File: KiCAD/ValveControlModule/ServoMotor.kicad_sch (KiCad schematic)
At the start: 5 parts, among them J1 DF51A-4P-2DS, U2 LT1785xS8

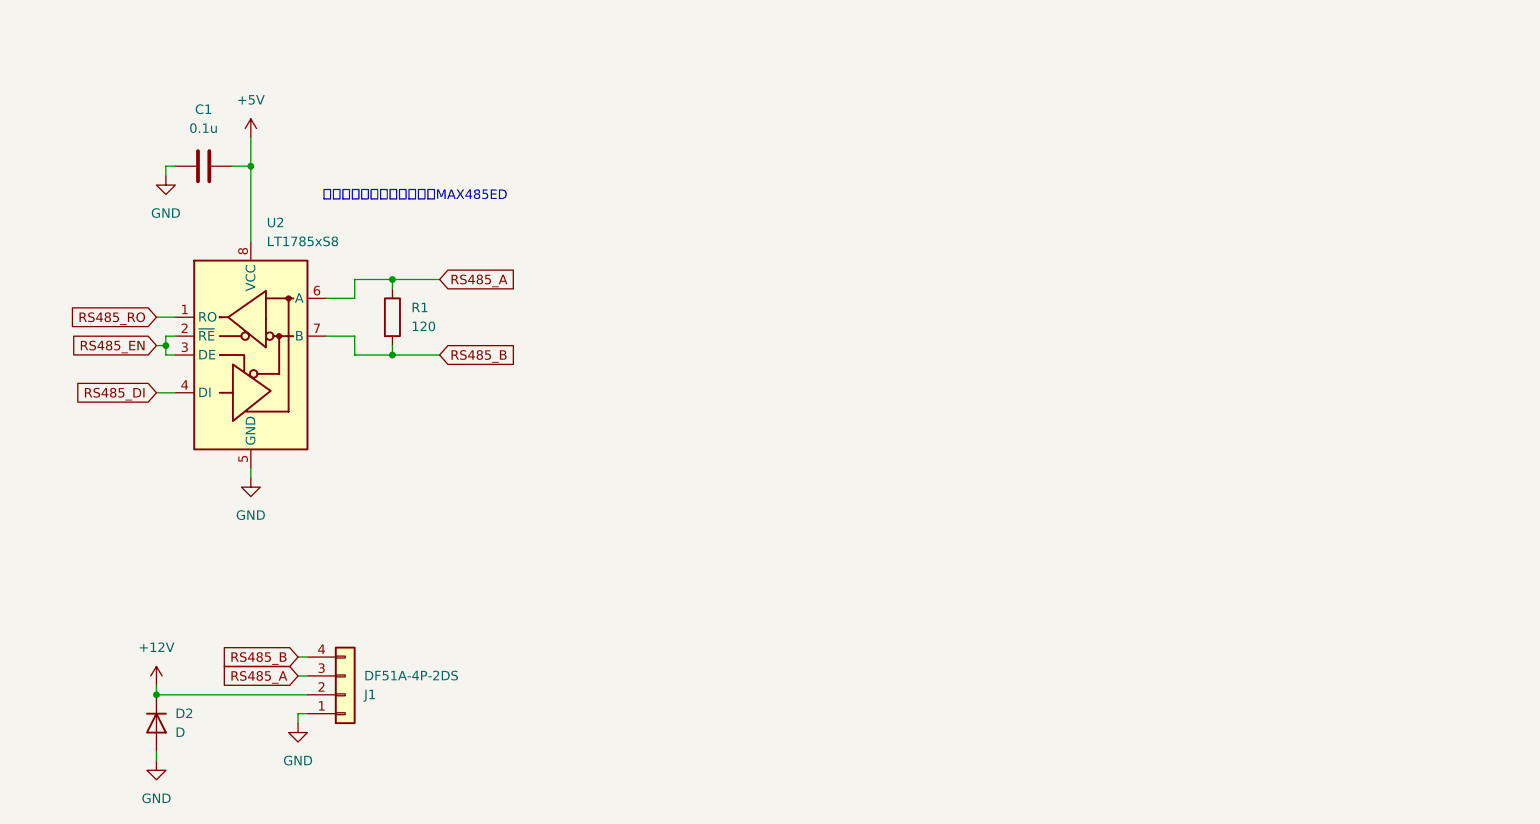
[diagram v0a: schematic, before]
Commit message: 電源，RS485の仕様を確定
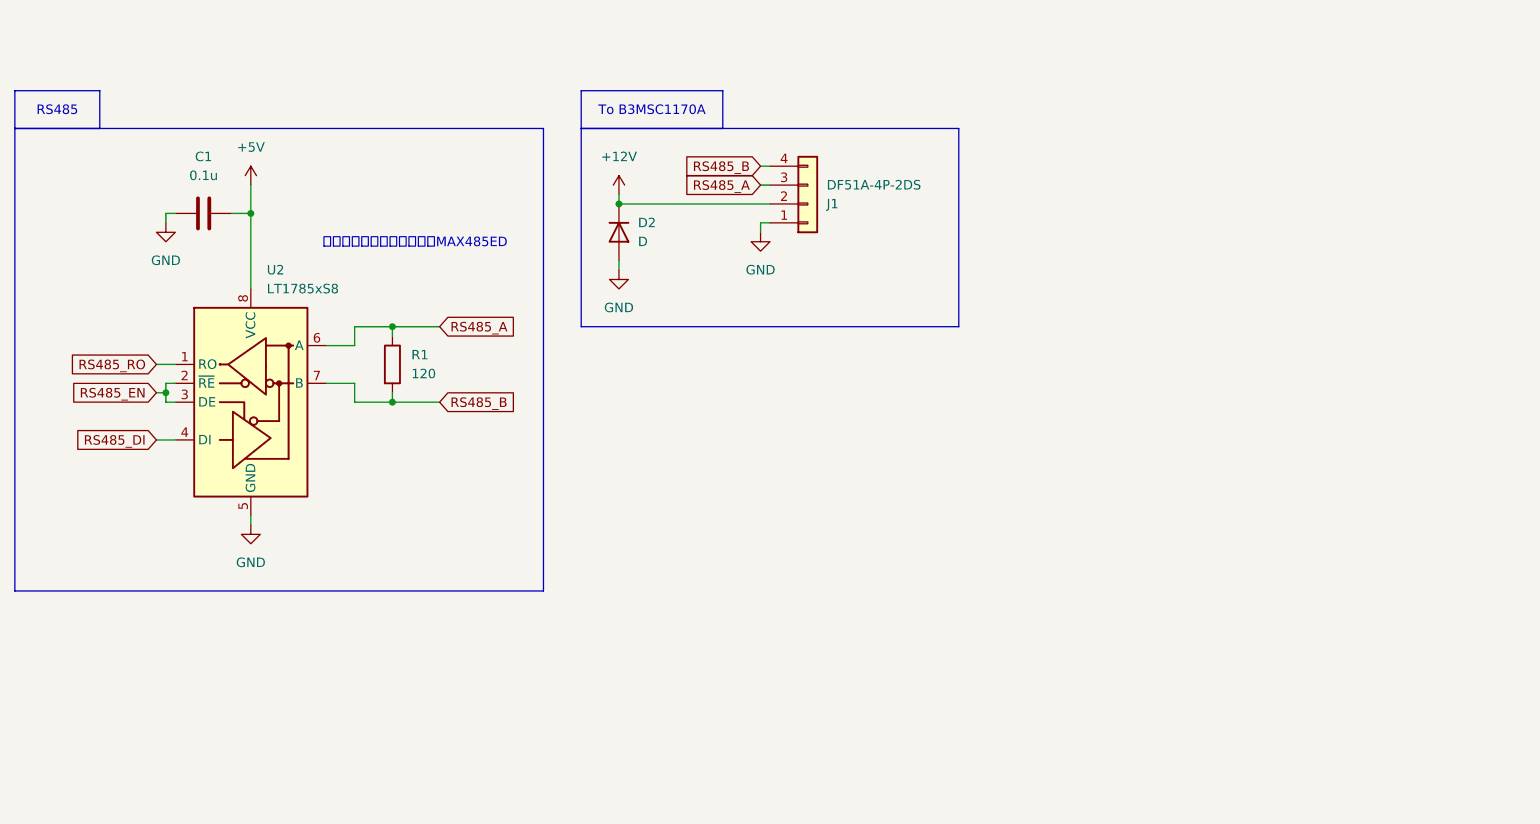
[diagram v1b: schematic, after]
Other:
- moved on the sheet: C1, D2, J1, R1, U2

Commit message: 取り付け穴位置を更新
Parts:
- C1: value 0.1u -> 0.1uF
- D2: value D -> SB34AFC; footprint (none) -> Diode_SMD:D_SMA_Handsoldering
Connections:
- net +5V renamed +3.3V
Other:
- note added: "ピンコンパチなので本当はLTC1480"
- note removed: "ピンコンパチなので本当はMAX485ED"
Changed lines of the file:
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@@
 		)
 	)
-	(text "ピンコンパチなので本当はMAX485ED"
+	(text "ピンコンパチなので本当はLTC1480"
 		(exclude_from_sim no)
 		(at 79.248 40.894 0)
@@
 			)
 		)
-		(property "Datasheet" "https://akizukidenshi.com/catalog/g/g116568/"
+		(property "Datasheet" "https://www.analog.com/media/en/technical-documentation/data-sheets/1480fa.pdf"
 			(at 44.45 59.69 0)
 			(effects
@@
 			)
 		)
-		(property "Value" "D"
+		(property "Value" "SB34AFC"
 			(at 109.22 40.6399 90)
 			(effects
@@
 			)
 		)
-		(property "Footprint" ""
+		(property "Footprint" "Diode_SMD:D_SMA_Handsoldering"
 			(at 106.68 39.37 0)
 			(effects
@@
 			)
 		)
-		(property "Datasheet" "~"
+		(property "Datasheet" "https://akizukidenshi.com/catalog/g/g106125/"
 			(at 106.68 39.37 0)
 			(effects
@@
 	)
 	(symbol
-		(lib_id "power:+5V")
-		(at 57.15 33.02 0)
+		(lib_id "Device:C")
+		(at 50.8 36.83 90)
 		(unit 1)
 		(exclude_from_sim no)
@@
 		(dnp no)
 		(fields_autoplaced yes)
+		(property "Reference" "C1"
+			(at 50.8 29.21 90)
+			(effects
+				(font
+					(size 1.27 1.27)
+				)
+			)
+		)
+		(property "Value" "0.1uF"
+			(at 50.8 31.75 90)
+			(effects
+				(font
+					(size 1.27 1.27)
+				)
+			)
+		)
+		(property "Footprint" "Capacitor_SMD:C_0603_1608Metric_Pad1.08x0.95mm_HandSolder"
+			(at 54.61 35.8648 0)
+			(effects
+				(font
+					(size 1.27 1.27)
+				)
+				(hide yes)
+			)
+		)
+		(property "Datasheet" "https://akizukidenshi.com/catalog/g/g113374/"
+			(at 50.8 36.83 0)
+			(effects
+				(font
+					(size 1.27 1.27)
+				)
+				(hide yes)
+			)
+		)
+		(property "Description" "Unpolarized capacitor"
+			(at 50.8 36.83 0)
+			(effects
+				(font
+					(size 1.27 1.27)
+				)
+				(hide yes)
+			)
+		)
+		(pin "2"
+		)
+		(pin "1"
+		)
+		(instances
+			(project ""
+				(path "/cd791ee8-0dde-470b-85a8-76474a846dd3/1a4e5e05-0a78-4189-a4ff-f4de07798bc1"
+					(reference "C1")
+					(unit 1)
+				)
+			)
+		)
+	)
+	(symbol
+		(lib_id "power:GND")
+		(at 125.73 39.37 0)
+		(unit 1)
+		(exclude_from_sim no)
+		(in_bom yes)
+		(on_board yes)
+		(dnp no)
+		(fields_autoplaced yes)
+		(property "Reference" "#PWR09"
+			(at 125.73 45.72 0)
+			(effects
+				(font
+					(size 1.27 1.27)
+				)
+				(hide yes)
+			)
+		)
+		(property "Value" "GND"
+			(at 125.73 44.45 0)
+			(effects
+				(font
+					(size 1.27 1.27)
+				)
+			)
+		)
+		(property "Footprint" ""
+			(at 125.73 39.37 0)
+			(effects
+				(font
+					(size 1.27 1.27)
+				)
+				(hide yes)
+			)
+		)
+		(property "Datasheet" ""
+			(at 125.73 39.37 0)
+			(effects
+				(font
+					(size 1.27 1.27)
+				)
+				(hide yes)
+			)
+		)
+		(property "Description" "Power symbol creates a global label with name \"GND\" , ground"
+			(at 125.73 39.37 0)
+			(effects
+				(font
+					(size 1.27 1.27)
+				)
+				(hide yes)
+			)
+		)
+		(pin "1"
+		)
+		(instances
+			(project ""
+				(path "/cd791ee8-0dde-470b-85a8-76474a846dd3/1a4e5e05-0a78-4189-a4ff-f4de07798bc1"
+					(reference "#PWR09")
+					(unit 1)
+				)
+			)
+		)
+	)
+	(symbol
+		(lib_id "power:GND")
+		(at 45.72 38.1 0)
+		(unit 1)
+		(exclude_from_sim no)
+		(in_bom yes)
+		(on_board yes)
+		(dnp no)
+		(fields_autoplaced yes)
+		(property "Reference" "#PWR08"
+			(at 45.72 44.45 0)
+			(effects
+				(font
+					(size 1.27 1.27)
+				)
+				(hide yes)
+			)
+		)
+		(property "Value" "GND"
+			(at 45.72 43.18 0)
+			(effects
+				(font
+					(size 1.27 1.27)
+				)
+			)
+		)
+		(property "Footprint" ""
+			(at 45.72 38.1 0)
+			(effects
+				(font
+					(size 1.27 1.27)
+				)
+				(hide yes)
+			)
+		)
+		(property "Datasheet" ""
+			(at 45.72 38.1 0)
+			(effects
+				(font
+					(size 1.27 1.27)
+				)
+				(hide yes)
+			)
+		)
+		(property "Description" "Power symbol creates a global label with name \"GND\" , ground"
+			(at 45.72 38.1 0)
+			(effects
+				(font
+					(size 1.27 1.27)
+				)
+				(hide yes)
+			)
+		)
+		(pin "1"
+		)
+		(instances
+			(project ""
+				(path "/cd791ee8-0dde-470b-85a8-76474a846dd3/1a4e5e05-0a78-4189-a4ff-f4de07798bc1"
+					(reference "#PWR08")
+					(unit 1)
+				)
+			)
+		)
+	)
+	(symbol
+		(lib_id "power:+3.3V")
+		(at 57.15 33.02 0)
+		(unit 1)
+		(exclude_from_sim no)
+		(in_bom yes)
+		(on_board yes)
+		(dnp no)
+		(fields_autoplaced yes)
 		(property "Reference" "#PWR06"
 			(at 57.15 36.83 0)
@@
 			)
 		)
-		(property "Value" "+5V"
+		(property "Value" "+3.3V"
 			(at 57.15 27.94 0)
 			(effects
@@
 			)
 		)
-		(property "Description" "Power symbol creates a global label with name \"+5V\""
+		(property "Description" "Power symbol creates a global label with name \"+3.3V\""
 			(at 57.15 33.02 0)
 			(effects
@@
 					(unit 1)
 				)
-			)
-		)
-	)
-	(symbol
-		(lib_id "Device:C")
-		(at 50.8 36.83 90)
-		(unit 1)
-		(exclude_from_sim no)
-		(in_bom yes)
-		(on_board yes)
-		(dnp no)
-		(fields_autoplaced yes)
-		(property "Reference" "C1"
-			(at 50.8 29.21 90)
-			(effects
-				(font
-					(size 1.27 1.27)
-				)
-			)
-		)
-		(property "Value" "0.1u"
-			(at 50.8 31.75 90)
-			(effects
-				(font
-					(size 1.27 1.27)
-				)
-			)
-		)
-		(property "Footprint" "Capacitor_SMD:C_0603_1608Metric_Pad1.08x0.95mm_HandSolder"
-			(at 54.61 35.8648 0)
-			(effects
-				(font
-					(size 1.27 1.27)
-				)
-				(hide yes)
-			)
-		)
-		(property "Datasheet" "~"
-			(at 50.8 36.83 0)
-			(effects
-				(font
-					(size 1.27 1.27)
-				)
-				(hide yes)
-			)
-		)
-		(property "Description" "Unpolarized capacitor"
-			(at 50.8 36.83 0)
-			(effects
-				(font
-					(size 1.27 1.27)
-				)
-				(hide yes)
-			)
-		)
-		(pin "2"
-		)
-		(pin "1"
-		)
-		(instances
-			(project ""
-				(path "/cd791ee8-0dde-470b-85a8-76474a846dd3/1a4e5e05-0a78-4189-a4ff-f4de07798bc1"
-					(reference "C1")
-					(unit 1)
-				)
-			)
-		)
-	)
-	(symbol
-		(lib_id "power:GND")
-		(at 125.73 39.37 0)
-		(unit 1)
-		(exclude_from_sim no)
-		(in_bom yes)
-		(on_board yes)
-		(dnp no)
-		(fields_autoplaced yes)
-		(property "Reference" "#PWR09"
-			(at 125.73 45.72 0)
-			(effects
-				(font
-					(size 1.27 1.27)
-				)
-				(hide yes)
-			)
-		)
-		(property "Value" "GND"
-			(at 125.73 44.45 0)
-			(effects
-				(font
-					(size 1.27 1.27)
-				)
-			)
-		)
-		(property "Footprint" ""
-			(at 125.73 39.37 0)
-			(effects
-				(font
-					(size 1.27 1.27)
-				)
-				(hide yes)
-			)
-		)
-		(property "Datasheet" ""
-			(at 125.73 39.37 0)
-			(effects
-				(font
-					(size 1.27 1.27)
-				)
-				(hide yes)
-			)
-		)
-		(property "Description" "Power symbol creates a global label with name \"GND\" , ground"
-			(at 125.73 39.37 0)
-			(effects
-				(font
-					(size 1.27 1.27)
-				)
-				(hide yes)
-			)
-		)
-		(pin "1"
-		)
-		(instances
-			(project ""
-				(path "/cd791ee8-0dde-470b-85a8-76474a846dd3/1a4e5e05-0a78-4189-a4ff-f4de07798bc1"
-					(reference "#PWR09")
-					(unit 1)
-				)
-			)
-		)
-	)
-	(symbol
-		(lib_id "power:GND")
-		(at 45.72 38.1 0)
-		(unit 1)
-		(exclude_from_sim no)
-		(in_bom yes)
-		(on_board yes)
-		(dnp no)
-		(fields_autoplaced yes)
-		(property "Reference" "#PWR08"
-			(at 45.72 44.45 0)
-			(effects
-				(font
-					(size 1.27 1.27)
-				)
-				(hide yes)
-			)
-		)
-		(property "Value" "GND"
-			(at 45.72 43.18 0)
-			(effects
-				(font
-					(size 1.27 1.27)
-				)
-			)
-		)
-		(property "Footprint" ""
-			(at 45.72 38.1 0)
-			(effects
-				(font
-					(size 1.27 1.27)
-				)
-				(hide yes)
-			)
-		)
-		(property "Datasheet" ""
-			(at 45.72 38.1 0)
-			(effects
-				(font
-					(size 1.27 1.27)
-				)
-				(hide yes)
-			)
-		)
-		(property "Description" "Power symbol creates a global label with name \"GND\" , ground"
-			(at 45.72 38.1 0)
-			(effects
-				(font
-					(size 1.27 1.27)
-				)
-				(hide yes)
-			)
-		)
-		(pin "1"
-		)
-		(instances
-			(project ""
-				(path "/cd791ee8-0dde-470b-85a8-76474a846dd3/1a4e5e05-0a78-4189-a4ff-f4de07798bc1"
-					(reference "#PWR08")
-					(unit 1)
-				)

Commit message: Build-2完成．発注．
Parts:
- removed D2: SB34AFC, Diode_SMD:D_SMA_Handsoldering, symbol Device:D
- added C16: 100uF, Capacitor_THT:CP_Radial_D8.0mm_P3.50mm, symbol Device:C_Polarized
- added C17: 22uF, Capacitor_SMD:C_0805_2012Metric_Pad1.18x1.45mm_HandSolder, symbol Device:C_Small
- added D1: SMAJ45A, Diode_SMD:D_SMA, symbol Device:D
- added Q1: AO3400A, Package_TO_SOT_SMD:SOT-23_Handsoldering, symbol Simulation_SPICE:NMOS
- added Q2, Q4: AO3401A, Package_TO_SOT_SMD:SOT-23_Handsoldering, symbol Transistor_FET:QM6015D
- added R10: 820R, Resistor_SMD:R_0603_1608Metric_Pad0.98x0.95mm_HandSolder, symbol Device:R_Small
- added R12: 10kR, Resistor_SMD:R_0603_1608Metric_Pad0.98x0.95mm_HandSolder, symbol Device:R_Small
- added R13: 100kR, Resistor_SMD:R_0603_1608Metric_Pad0.98x0.95mm_HandSolder, symbol Device:R_Small
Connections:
- net +12V: now also C16.1, C17.1, D1.1 (K), Q2.3 (S), R12.1; no longer J1.2 (Pin_2)
- net GND: now also C16.2, D1.2 (A), Q1.3 (S)
- new net: C17.2, Q2.1 (G), Q4.1 (G), R12.2, R13.1
- new net: Q2.2 (D), Q4.2 (D)
- new net: Q1.1 (D), R13.2
- new net: Q1.2 (G), R10.2
- new net: J1.2 (Pin_2), Q4.3 (S)
- new net ServoPower_EN: R10.1
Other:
- moved on the sheet: J1

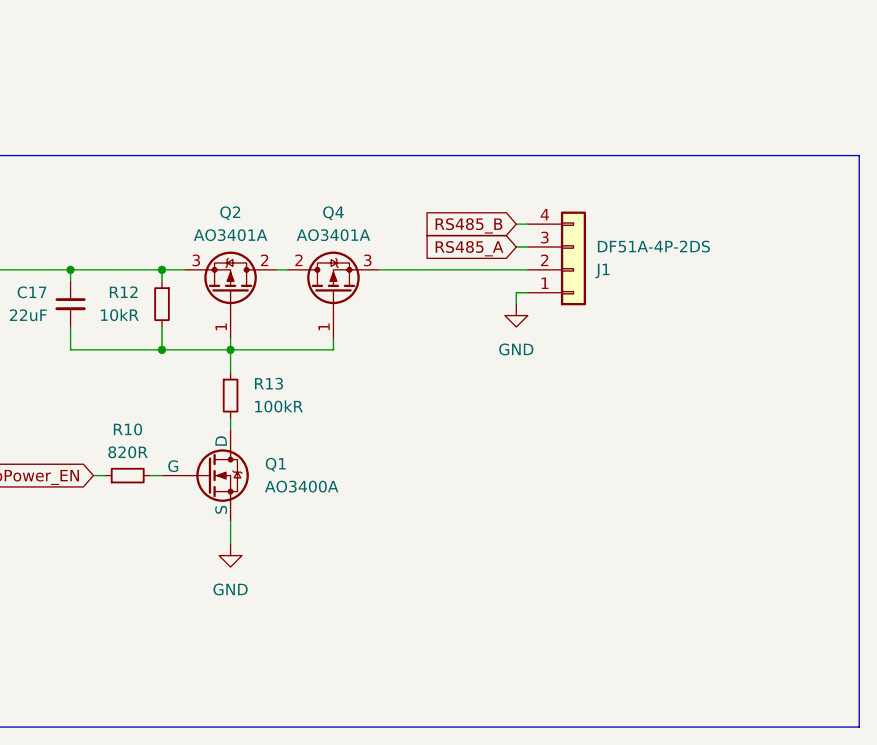
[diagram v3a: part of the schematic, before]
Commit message: MOSFET周りのフットプリント，回路図を修正
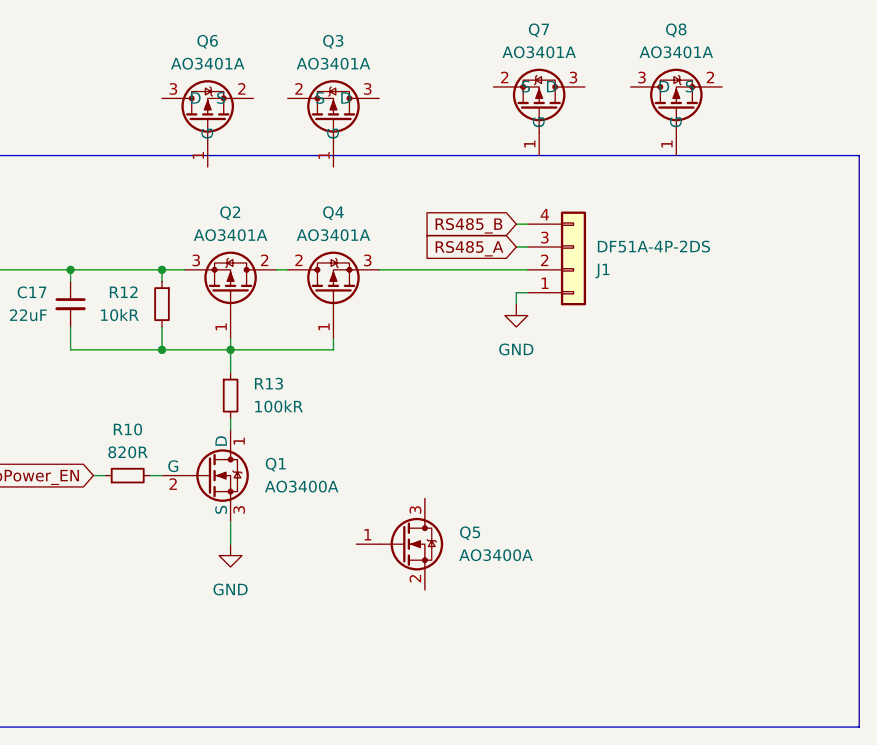
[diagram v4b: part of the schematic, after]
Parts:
- added Q3, Q6, Q7, Q8: AO3401A, Package_TO_SOT_SMD:SOT-23, symbol Transistor_FET:AO3401A
- added Q5: AO3400A, Package_TO_SOT_SMD:SOT-23, symbol Transistor_FET:AO3400A

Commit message: Build-3発注済み
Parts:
- removed Q1: AO3400A, Package_TO_SOT_SMD:SOT-23_Handsoldering, symbol Simulation_SPICE:NMOS
- removed Q2, Q4: AO3401A, Package_TO_SOT_SMD:SOT-23_Handsoldering, symbol Transistor_FET:QM6015D
- removed Q3, Q6, Q7, Q8: AO3401A, Package_TO_SOT_SMD:SOT-23, symbol Transistor_FET:AO3401A
- removed Q5: AO3400A, Package_TO_SOT_SMD:SOT-23, symbol Transistor_FET:AO3400A
- added Q2, Q4: AO3401A, Package_TO_SOT_SMD:SOT-23_Handsoldering, symbol Transistor_FET:AO3401A
- added Q3: AO3400A, Package_TO_SOT_SMD:SOT-23_Handsoldering, symbol Transistor_FET:AO3400A
- added R14: 10kR, Resistor_SMD:R_0603_1608Metric_Pad0.98x0.95mm_HandSolder, symbol Device:R_Small
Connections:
- net +12V: now also Q4.2 (S)
- net GND: now also Q3.2 (S), R14.2
- net at C17.2, R12.2, R13.1: now also Q2.1 (G), Q4.1 (G)
- net at R13.2: now also Q3.3 (D)
- net at R10.2: now also Q3.1 (G), R14.1
- net at J1.2 (Pin_2): now also Q2.2 (S)
- new net: Q2.3 (D), Q4.3 (D)
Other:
- moved on the sheet: R10
